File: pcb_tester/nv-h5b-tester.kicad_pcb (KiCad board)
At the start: 2 copper layers, 8 x 20 mm, 17 parts, among them J1 PSH02-03, J2 Conn_01x01, J3 Conn_01x01, J4 Conn_01x01, J5 Conn_01x01, J6 Conn_01x01, J7 Conn_01x01, U1 ATtiny25-20SS

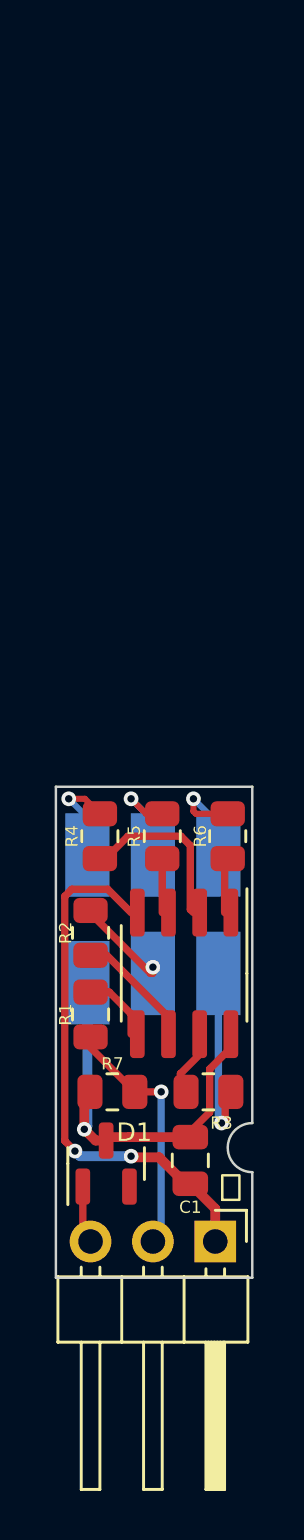
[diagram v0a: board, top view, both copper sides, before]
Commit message: Tester: add LEDs to chematics, route PCB.
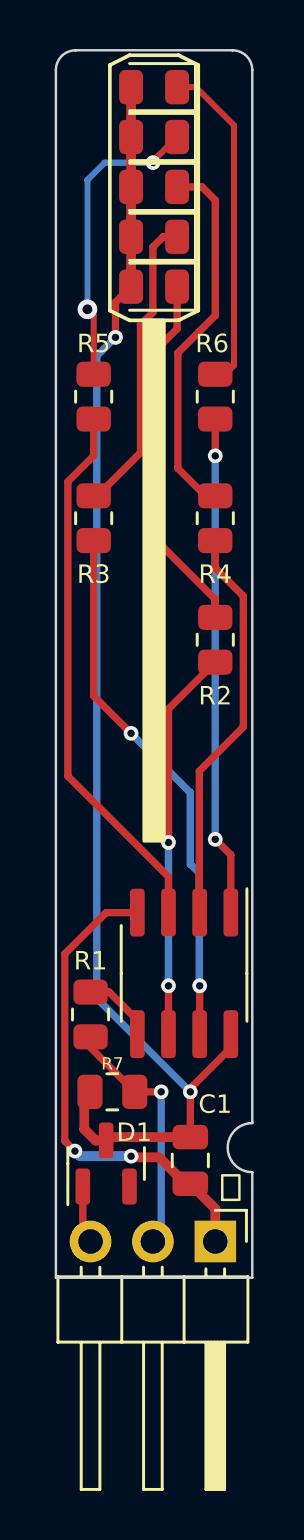
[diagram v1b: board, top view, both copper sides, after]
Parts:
- removed J2, J3, J4, J5, J6, J7: Conn_01x01, TestPoint:TestPoint_Keystone_5015_Micro-Minature
- added D2: YELLOW, LED_SMD:LED_0805_2012Metric, F.Cu at (124.0, 89.6)
- added D3: WHITE, LED_SMD:LED_0805_2012Metric, F.Cu at (124.0, 87.6)
- added D4: RED, LED_SMD:LED_0805_2012Metric, F.Cu at (124.0, 85.6)
- added D5: GREEN, LED_SMD:LED_0805_2012Metric, F.Cu at (124.0, 83.5)
- added D6: YELLOW, LED_SMD:LED_0805_2012Metric, F.Cu at (124.0, 81.5)
- moved R3 23.8 mm to (121.5, 99.1), turned to -90 degrees
- moved R5 18.1 mm to (121.5, 94.1)
- moved R6 17.9 mm to (126.5, 94.1)
- moved R4 13.8 mm to (126.5, 99.1)
- moved R2 13.0 mm to (126.5, 104.0), turned to 90 degrees
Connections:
- R2 pad 1: /LED_YEL_BOT -> /dLED_YEL_BOT
- R2 pad 2: /dLED_YEL_BOT -> /LED_YEL_BOT
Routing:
- net VCC: track 17.1 -> 54.1 mm, vias 1 -> 2
- net /dLED_GR: track 2.20 -> 22.2 mm
- net /dLED_WHITE: track 2.68 -> 21.9 mm, vias 0 -> 2
- net /dLED_YEL_TOP: track 2.25 -> 20.4 mm, vias 0 -> 2
- net /LED_YEL_BOT: track 3.67 -> 14.8 mm, vias 1 -> 0
- net /dLED_YEL_BOT: track 4.91 -> 15.9 mm, vias 0 -> 2
- net /LED_YEL_TOP: track 3.92 -> 13.7 mm, vias 1 -> 0
- net /LED_RED: track 5.67 -> 15.3 mm, vias 1 -> 0
- net /dLED_RED: track 7.00 -> 16.4 mm
- net /LED_GR: track 4.18 -> 12.4 mm, vias 1 -> 2
- net /LED_WHITE: track 7.48 -> 12.4 mm, vias 1 -> 0
- net GND: track 21.8 -> 19.7 mm
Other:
- board size 8 x 20 mm -> 8 x 50 mm
- board text added: "NV-H5b tester v1.0"
- board text removed: "NV-H5b v3.0"
- board text removed: "bílá"
- board text removed: "zelená"
- board text removed: "červ."
- board text removed: "žldol."
- board text removed: "žlhor."

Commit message: Use thin top width.
Because signal must fit in tracks profile.
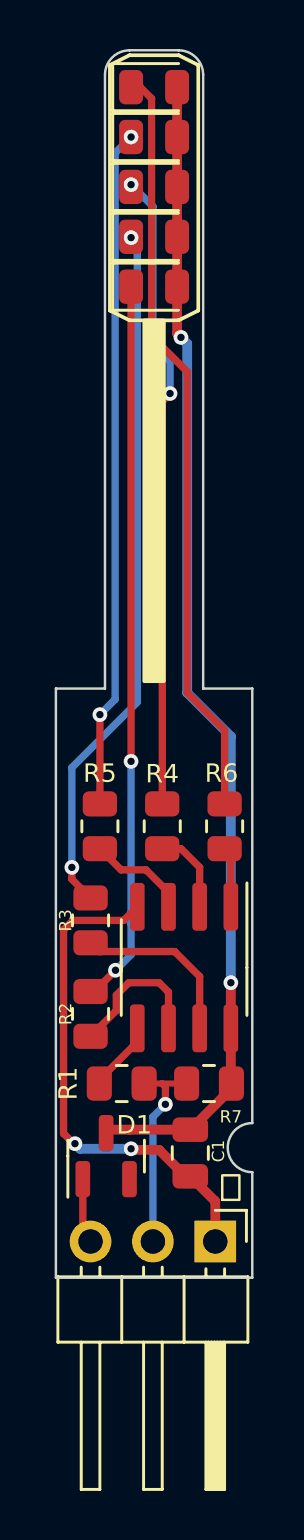
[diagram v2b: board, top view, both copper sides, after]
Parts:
- moved R6 17.5 mm to (126.9, 111.6)
- moved R5 17.5 mm to (121.8, 111.6)
- moved R3 16.4 mm to (121.4, 115.4)
- moved R2 16.1 mm to (121.4, 119.3)
- moved R4 12.7 mm to (124.3, 111.6)
- moved R7 3.95 mm to (126.2, 122.1), turned to 180 degrees
- moved R1 3.09 mm to (122.7, 122.1), turned to 180 degrees
- moved D1 0.30 mm to (122.0, 125.0)
- moved C1 0.30 mm to (125.5, 124.9)
- moved U1 0.24 mm to (125.2, 117.4)
- turned D2 to 0 degrees
- turned D3 to 0 degrees
- turned D4 to 0 degrees
- turned D5 to 0 degrees
- turned D6 to 0 degrees
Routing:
- net /dLED_GR: track 22.2 -> 4.12 mm
- net /dLED_YEL_TOP: track 20.4 -> 2.58 mm, vias 2 -> 0
- net /LED_YEL_TOP: track 13.7 -> 31.0 mm
- net /LED_WHITE: track 12.4 -> 28.5 mm, vias 0 -> 2
- net /LED_GR: track 12.4 -> 27.7 mm
- net /dLED_WHITE: track 21.9 -> 7.13 mm, vias 2 -> 0
- net /LED_YEL_BOT: track 14.8 -> 29.5 mm, vias 0 -> 2
- net /dLED_RED: track 16.4 -> 3.45 mm
- net /LED_RED: track 15.3 -> 26.1 mm, vias 0 -> 2
- net /dLED_YEL_BOT: track 15.9 -> 6.08 mm, vias 2 -> 0
- net VCC: track 54.1 -> 47.6 mm
- net /DATA_IN: track 10.3 -> 8.43 mm
- net GND: track 19.7 -> 20.7 mm
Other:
- outline, holes or cut-outs redrawn
